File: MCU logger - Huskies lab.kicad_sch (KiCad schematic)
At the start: 25 parts, among them U1 ATMEGA328P-AU, U2 DS1337S+, U3 24LC1025, U4 24LC1025, Y1 32.768KHz, Y2 16Mhz

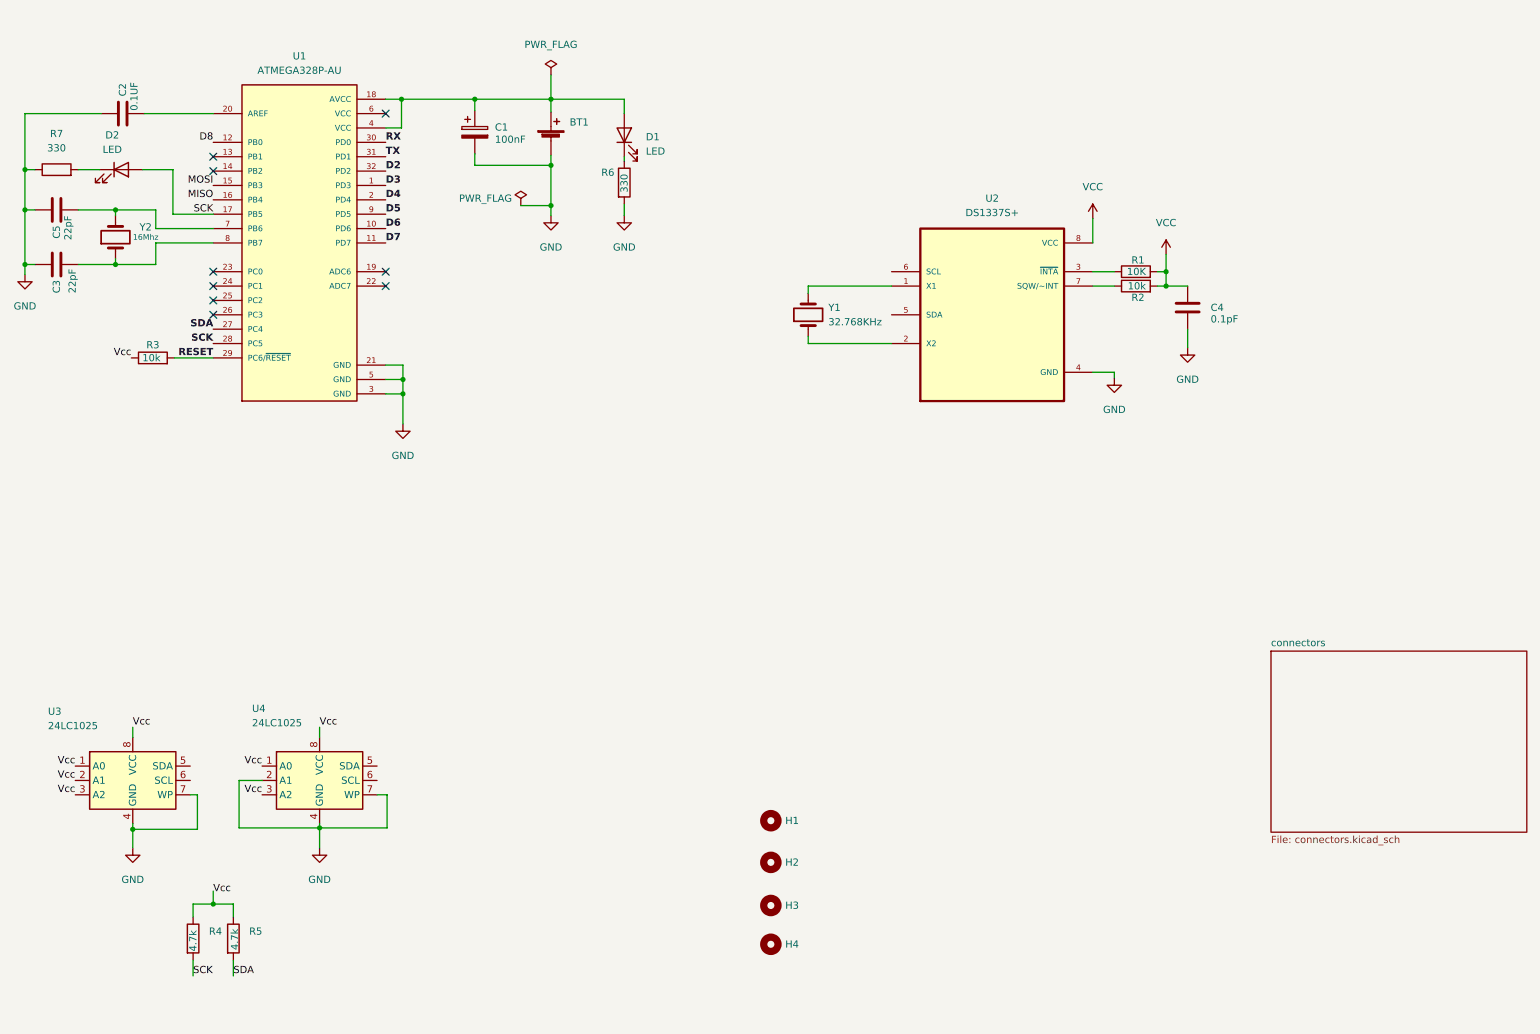
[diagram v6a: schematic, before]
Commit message: cableado c asi terminado, dos error aun
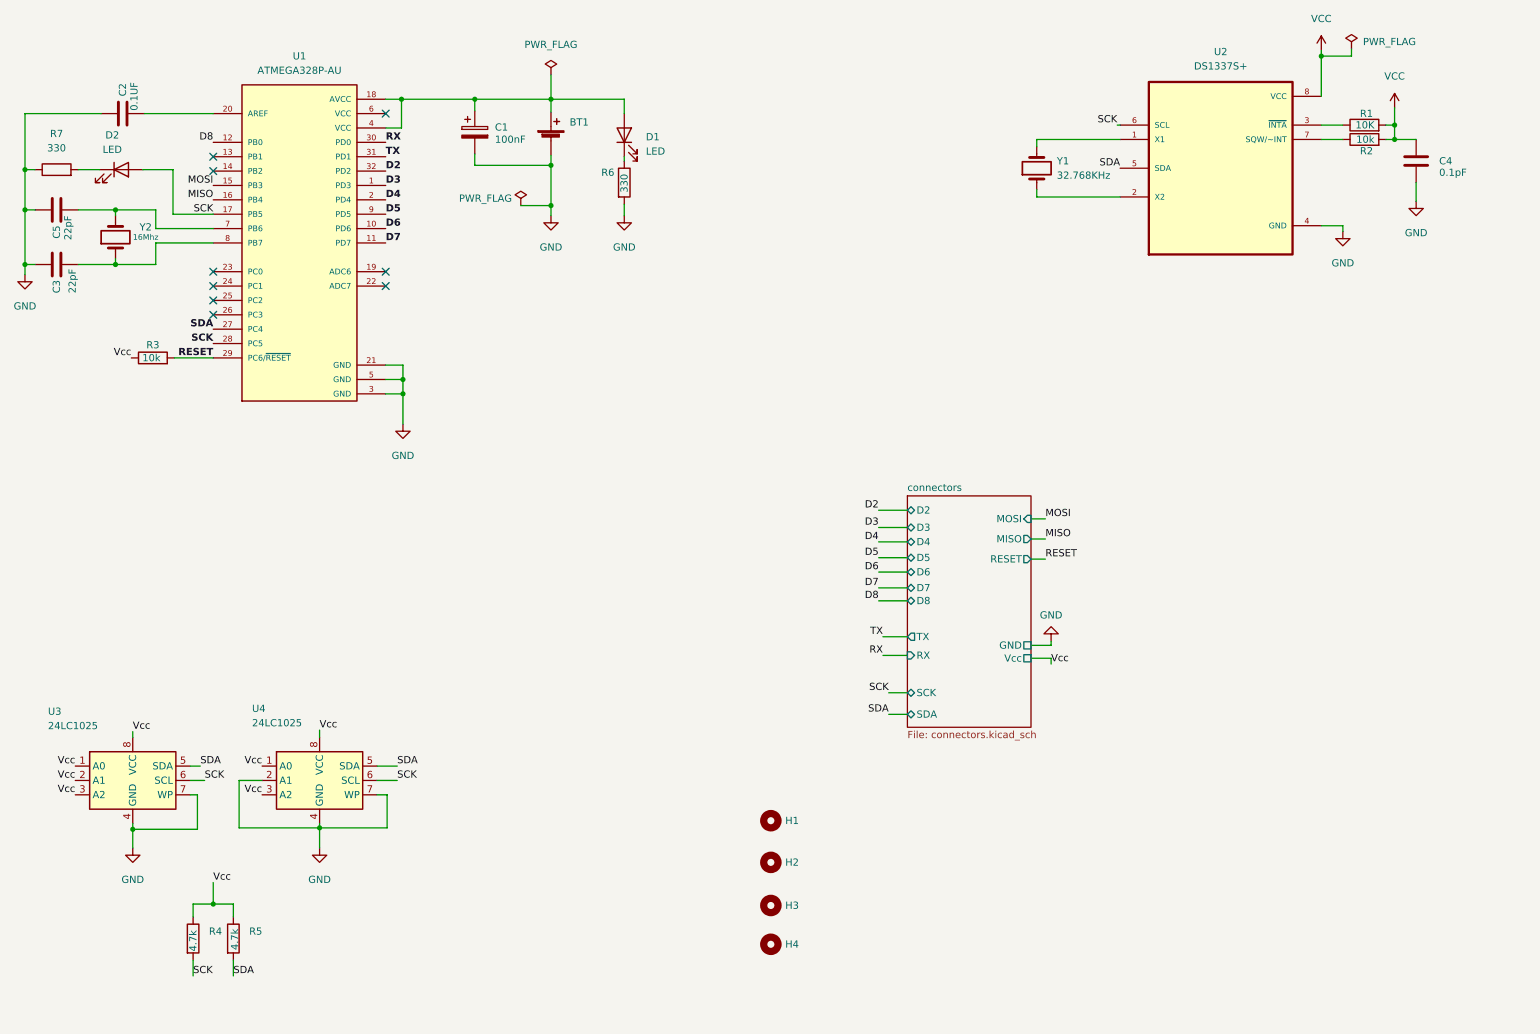
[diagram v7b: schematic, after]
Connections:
- net SCK: now also U2.6 (SCL), U3.6 (SCL), U4.6 (SCL)
- net SDA: now also U2.5 (SDA), U3.5 (SDA), U4.5 (SDA)
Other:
- sheet connectors ports: added D2, D3, D4, D5, D6, D7, D8, GND, MISO, MOSI, RESET, RX, SCK, SDA, TX, Vcc; removed none
- moved on the sheet: C4, R1, R2, U2, Y1

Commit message: cambio de nombre a las etiquetas, de Vcc a VCC, para que todas las etiquetas tengan el mismo nombre
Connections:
- net Vcc is gone; now on net VCC: R3.1, R4.1, R5.1, U3.1 (A0), U3.2 (A1), U3.3 (A2), U3.8 (VCC), U4.1 (A0), U4.3 (A2), U4.8 (VCC)
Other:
- sheet connectors ports: added VCC; removed Vcc
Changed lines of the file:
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@@
   (junction (at 18.034 46.99) (diameter 0) (color 0 0 0 0)
   )
+  (junction (at 247.142 29.464) (diameter 0) (color 0 0 0 0)
+  )
   (junction (at 84.582 34.544) (diameter 0) (color 0 0 0 0)
   )
   (junction (at 110.998 34.544) (diameter 0) (color 0 0 0 0)
-  )
-  (junction (at 247.142 26.924) (diameter 0) (color 0 0 0 0)
   )
   (junction (at 110.998 46.228) (diameter 0) (color 0 0 0 0)
@@
     (stroke (width 0) (type default) (color 0 0 0 0))
   )
-  (wire (pts (xy 247.142 26.924) (xy 252.476 26.924))
-    (stroke (width 0) (type default) (color 0 0 0 0))
-  )
   (wire (pts (xy 18.034 37.084) (xy 18.034 46.99))
     (stroke (width 0) (type default) (color 0 0 0 0))
@@
     (stroke (width 0) (type default) (color 0 0 0 0))
   )
-  (wire (pts (xy 252.476 25.654) (xy 252.476 26.924))
-    (stroke (width 0) (type default) (color 0 0 0 0))
-  )
   (wire (pts (xy 80.264 157.48) (xy 82.042 157.48))
     (stroke (width 0) (type default) (color 0 0 0 0))
   )
+  (wire (pts (xy 238.76 29.464) (xy 247.142 29.464))
+    (stroke (width 0) (type default) (color 0 0 0 0))
+  )
   (wire (pts (xy 70.104 163.322) (xy 70.104 166.878))
     (stroke (width 0) (type default) (color 0 0 0 0))
@@
     (stroke (width 0) (type default) (color 0 0 0 0))
   )
+  (wire (pts (xy 247.142 29.464) (xy 247.142 34.036))
+    (stroke (width 0) (type default) (color 0 0 0 0))
+  )
   (wire (pts (xy 199.39 133.35) (xy 199.39 134.366))
     (stroke (width 0) (type default) (color 0 0 0 0))
@@
     (stroke (width 0) (type default) (color 0 0 0 0))
   )
-  (wire (pts (xy 70.104 147.32) (xy 70.104 146.05))
+  (wire (pts (xy 70.104 147.32) (xy 69.85 146.304))
     (stroke (width 0) (type default) (color 0 0 0 0))
   )
@@
     (stroke (width 0) (type default) (color 0 0 0 0))
   )
-  (wire (pts (xy 247.142 26.924) (xy 247.142 34.036))
-    (stroke (width 0) (type default) (color 0 0 0 0))
-  )
   (wire (pts (xy 110.998 34.544) (xy 123.952 34.544))
     (stroke (width 0) (type default) (color 0 0 0 0))
@@
     (stroke (width 0) (type default) (color 0 0 0 0))
   )
+  (wire (pts (xy 247.142 28.194) (xy 247.142 29.464))
+    (stroke (width 0) (type default) (color 0 0 0 0))
+  )
   (wire (pts (xy 250.952 56.896) (xy 250.952 57.912))
     (stroke (width 0) (type default) (color 0 0 0 0))
@@
     (stroke (width 0) (type default) (color 0 0 0 0))
   )
-  (wire (pts (xy 247.142 25.908) (xy 247.142 26.924))
-    (stroke (width 0) (type default) (color 0 0 0 0))
-  )
   (wire (pts (xy 199.39 130.302) (xy 199.39 131.064))
     (stroke (width 0) (type default) (color 0 0 0 0))
@@
   )
   (wire (pts (xy 18.034 63.754) (xy 19.812 63.754))
+    (stroke (width 0) (type default) (color 0 0 0 0))
+  )
+  (wire (pts (xy 238.76 27.94) (xy 238.76 29.464))
     (stroke (width 0) (type default) (color 0 0 0 0))
   )
@@
     (effects (font (size 1.27 1.27)) (justify left bottom))
   )
-  (label "Vcc" (at 70.104 146.05 0)
+  (label "VCC" (at 69.85 146.304 0)
     (effects (font (size 1.27 1.27)) (justify left bottom))
   )
@@
     (effects (font (size 1.27 1.27)) (justify right bottom))
   )
-  (label "Vcc" (at 199.39 134.366 0)
+  (label "VCC" (at 199.39 134.366 0)
     (effects (font (size 1.27 1.27)) (justify left bottom))
   )
@@
     (effects (font (size 1.27 1.27)) (justify right bottom))
   )
-  (label "Vcc" (at 26.924 152.4 180)
+  (label "VCC" (at 26.924 152.4 180)
     (effects (font (size 1.27 1.27)) (justify right bottom))
   )
@@
     (effects (font (size 1.27 1.27)) (justify right bottom))
   )
-  (label "Vcc" (at 51.308 172.974 0)
+  (label "VCC" (at 51.308 172.974 0)
     (effects (font (size 1.27 1.27)) (justify left bottom))
   )
@@
     (effects (font (size 1.27 1.27) bold) (justify left bottom))
   )
-  (label "Vcc" (at 59.944 152.4 180)
+  (label "VCC" (at 59.944 152.4 180)
     (effects (font (size 1.27 1.27)) (justify right bottom))
   )
@@
     (effects (font (size 1.27 1.27)) (justify left bottom))
   )
-  (label "Vcc" (at 26.924 154.94 180)
+  (label "VCC" (at 26.924 154.94 180)
     (effects (font (size 1.27 1.27)) (justify right bottom))
   )
@@
     (effects (font (size 1.27 1.27)) (justify left bottom))
   )
-  (label "Vcc" (at 37.084 146.304 0)
+  (label "VCC" (at 37.084 146.304 0)
     (effects (font (size 1.27 1.27)) (justify left bottom))
   )
@@
     (effects (font (size 1.27 1.27)) (justify left bottom))
   )
-  (label "Vcc" (at 59.944 157.48 180)
+  (label "VCC" (at 59.944 157.48 180)
     (effects (font (size 1.27 1.27)) (justify right bottom))
   )
@@
     (effects (font (size 1.27 1.27) bold) (justify left bottom))
   )
-  (label "Vcc" (at 26.924 157.48 180)
+  (label "VCC" (at 26.924 157.48 180)
     (effects (font (size 1.27 1.27)) (justify right bottom))
   )
@@
     (effects (font (size 1.27 1.27) bold) (justify left bottom))
   )
-  (label "Vcc" (at 36.83 80.264 180)
+  (label "VCC" (at 36.83 80.264 180)
     (effects (font (size 1.27 1.27)) (justify right bottom))
   )
@@
     (pin "1")
     (pin "2")
-  )
-  (symbol (lib_id "power:PWR_FLAG") (at 252.476 25.654 0) (unit 1)
-    (in_bom yes) (on_board yes) (fields_autoplaced)
-    (property "Reference" "#FLG0103" (id 0) (at 252.476 23.749 0)
-      (effects (font (size 1.27 1.27)) hide)
-    )
-    (property "Value" "PWR_FLAG" (id 1) (at 254.508 24.3839 0)
-      (effects (font (size 1.27 1.27)) (justify left))
-    )
-    (property "Footprint" "" (id 2) (at 252.476 25.654 0)
-      (effects (font (size 1.27 1.27)) hide)
-    )
-    (property "Datasheet" "~" (id 3) (at 252.476 25.654 0)
-      (effects (font (size 1.27 1.27)) hide)
-    )
-    (pin "1")
   )
   (symbol (lib_id "Device:LED") (at 35.052 46.99 0) (unit 1)
@@
     (pin "1")
   )
+  (symbol (lib_id "power:VCC") (at 247.142 28.194 0) (unit 1)
+    (in_bom yes) (on_board yes) (fields_autoplaced)
+    (property "Reference" "#PWR0109" (id 0) (at 247.142 32.004 0)
+      (effects (font (size 1.27 1.27)) hide)
+    )
+    (property "Value" "VCC" (id 1) (at 247.142 22.606 0))
+    (property "Footprint" "" (id 2) (at 247.142 28.194 0)
+      (effects (font (size 1.27 1.27)) hide)
+    )
+    (property "Datasheet" "" (id 3) (at 247.142 28.194 0)
+      (effects (font (size 1.27 1.27)) hide)
+    )
+    (pin "1")
+  )
   (symbol (lib_id "Device:C") (at 263.906 45.466 0) (unit 1)
     (in_bom yes) (on_board yes)
@@
     (pin "1")
   )
-  (symbol (lib_id "power:VCC") (at 247.142 25.908 0) (unit 1)
-    (in_bom yes) (on_board yes) (fields_autoplaced)
-    (property "Reference" "#PWR0109" (id 0) (at 247.142 29.718 0)
-      (effects (font (size 1.27 1.27)) hide)
-    )
-    (property "Value" "VCC" (id 1) (at 247.142 20.32 0))
-    (property "Footprint" "" (id 2) (at 247.142 25.908 0)
-      (effects (font (size 1.27 1.27)) hide)
-    )
-    (property "Datasheet" "" (id 3) (at 247.142 25.908 0)
-      (effects (font (size 1.27 1.27)) hide)
-    )
-    (pin "1")
-  )
   (symbol (lib_id "power:VCC") (at 260.096 36.068 0) (unit 1)
     (in_bom yes) (on_board yes) (fields_autoplaced)
@@
     (pin "2")
   )
+  (symbol (lib_id "power:PWR_FLAG") (at 238.76 27.94 0) (unit 1)
+    (in_bom yes) (on_board yes) (fields_autoplaced)
+    (property "Reference" "#FLG0103" (id 0) (at 238.76 26.035 0)
+      (effects (font (size 1.27 1.27)) hide)
+    )
+    (property "Value" "PWR_FLAG" (id 1) (at 238.76 22.86 0))
+    (property "Footprint" "" (id 2) (at 238.76 27.94 0)
+      (effects (font (size 1.27 1.27)) hide)
+    )
+    (property "Datasheet" "~" (id 3) (at 238.76 27.94 0)
+      (effects (font (size 1.27 1.27)) hide)
+    )
+    (pin "1")
+  )
   (symbol (lib_id "Mechanical:MountingHole") (at 149.86 177.038 0) (unit 1)
     (in_bom yes) (on_board yes) (fields_autoplaced)
@@
       (effects (font (size 1.27 1.27)) (justify left top))
     )
-    (pin "Vcc" passive (at 195.834 133.35 0)
+    (pin "VCC" passive (at 195.834 133.35 0)
       (effects (font (size 1.27 1.27)) (justify right))
     )
@@
       (reference "#FLG0102") (unit 1) (value "PWR_FLAG") (footprint "")
     )
-    (path "/0413466f-97f4-4cf5-b43b-89041fe40270"
+    (path "/c45eb814-7b55-421e-8dde-df88ebe6364e"
       (reference "#FLG0103") (unit 1) (value "PWR_FLAG") (footprint "")
     )
@@
       (reference "#PWR0108") (unit 1) (value "VCC") (footprint "")
     )
-    (path "/653b2baa-3645-4fa1-aaee-cfc5e05a15da"
+    (path "/3c11b1e2-070b-4eb7-bd30-82f94f57554b"
       (reference "#PWR0109") (unit 1) (value "VCC") (footprint "")
     )
